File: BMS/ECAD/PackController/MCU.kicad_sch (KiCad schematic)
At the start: 51 parts, among them Q1 BC846, Q2 DMP4065S-7, U4 24LC256

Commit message: schematic finished, review tbd
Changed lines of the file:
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@@
+		)
+	)
+	(hierarchical_label "NTC1_Sig"
+		(shape input)
+		(at -19.05 182.88 180)
+		(effects
+			(font
+				(size 1.27 1.27)
+			)
+			(justify right)
 		)
 	)
@@
 		)
 	)
+	(hierarchical_label "NTC2_Sig"
+		(shape input)
+		(at -19.05 185.42 180)
+		(effects
+			(font
+				(size 1.27 1.27)
+			)
+			(justify right)
+		)
+	)
 	(hierarchical_label "UART_LS_TX"
 		(shape input)
@@
 		)
 	)
+	(hierarchical_label "NTC3_Sig"
+		(shape input)
+		(at -19.05 187.96 180)
+		(effects
+			(font
+				(size 1.27 1.27)
+			)
+			(justify right)
+		)
+	)
 	(hierarchical_label "AIR_P_Actual"
 		(shape input)
@@
 		)
 	)
+	(hierarchical_label "PCHRG_SWITCH"
+		(shape input)
+		(at -17.78 173.99 180)
+		(effects
+			(font
+				(size 1.27 1.27)
+			)
+			(justify right)
+		)
+	)
 	(hierarchical_label "Buzzer_CTRL"
 		(shape input)
@@
 		)
 	)
-	(hierarchical_label "DANGER_V"
+	(hierarchical_label "nDANGER_V"
 		(shape input)
 		(at -26.67 153.67 0)

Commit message: close to finish BMS master, only some footprints needed
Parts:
- removed D1, D2, D3, D4, D5: BAS16HT1, Diode_SMD:D_SOD-323_HandSoldering, symbol Diode:BAS16W
- removed Error1: LED Red, LED_SMD:LED_0805_2012Metric_Pad1.15x1.40mm_HandSolder, symbol Device:LED
- removed Heart?: LED Blue, LED_SMD:LED_0805_2012Metric_Pad1.15x1.40mm_HandSolder, symbol Device:LED
- removed R39: 1kR, Resistor_SMD:R_0603_1608Metric_Pad0.98x0.95mm_HandSolder, symbol Device:R
- removed R41, R42: 4.7kR, Resistor_SMD:R_0603_1608Metric_Pad0.98x0.95mm_HandSolder, symbol Device:R
- removed R9, R?: 100R 0603, Resistor_SMD:R_0603_1608Metric_Pad0.98x0.95mm_HandSolder, symbol Device:R
- removed R?: 20R 0603, Resistor_SMD:R_0603_1608Metric_Pad0.98x0.95mm_HandSolder, symbol Device:R
- added D201, D203, D204, D205, D206, D207, D209: BAT46, Diode_SMD:D_SOD-123, symbol Diode:BAT46
- added Error201: LED Red, LED_SMD:LED_0805_2012Metric_Pad1.15x1.40mm_HandSolder, symbol Device:LED
- added Heart201: LED Blue, LED_SMD:LED_0805_2012Metric_Pad1.15x1.40mm_HandSolder, symbol Device:LED
- added R203, R206, R208, R211, R213: 10kR, Resistor_SMD:R_0603_1608Metric_Pad0.98x0.95mm_HandSolder, symbol Device:R
- added R210, R212: 100R 0603, Resistor_SMD:R_0603_1608Metric_Pad0.98x0.95mm_HandSolder, symbol Device:R
- R214: renamed from R40; value 10kR -> 220kR
- U203: renamed from U6; value (none) -> SN74LVC1G74; footprint (none) -> Package_SO:VSSOP-8_2.3x2mm_P0.5mm
- U205: renamed from U4; value 24LC256 -> 24LC256-I/SN; footprint (none) -> Package_SO:SOIC-8_5.3x5.3mm_P1.27mm
- gave numbers to parts that had none: 22
- renumbered C20 to C208, C21 to C213, C19 to C214, Q2 to Q201, Q1 to Q202, R44 to R205, R43 to R207, R1 to R209, R2 to R216, R32 to R217, R33 to R218, R34 to R219, U5 to U202
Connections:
- net Heart_AFR is gone; now on net R_Leak1_Supply: U204.19 (PF2)
- net Reset_AFE is gone; now on net nRES: JTAG201.12 (Pin_12)
- net SC_Opening is gone; now on net SC_Latched: R214.1
- net +3.3V: now also R203.1, R206.1, R213.2
- net AIR_Error: now also U204.94 (PB7)
- net AIR_N_Actual: now also U204.93 (PB6)
- net AIR_N_Intended: now also U204.92 (PB5)
- net AIR_N_Switch: now also U204.86 (PD4)
- net AIR_P_Actual: now also U204.89 (PD7)
- net AIR_P_Intended: now also U204.88 (PD6)
- net AIR_P_Switch: now also U204.85 (PD3)
- net ERRQ: now also U204.61 (PD14)
- net ERRQ_Ioc_out: now also U204.57 (PD10)
- net ERRQ_ext: now also U204.59 (PD12)
- net ERRQ_ext_out: now also U204.58 (PD11)
- net ERRQ_res: now also U204.60 (PD13)
- net GND: now also R210.2, R211.1, R212.1
- net JTDO/SWO: now also U204.90 (PB3)
- net NTC1_Sig: now also U204.28 (PA6)
- net NTC2_Sig: now also U204.39 (PE8)
- net NTC3_Sig: now also U204.45 (PE14)
- net PCHRG_SWITCH: now also U204.82 (PD0)
- net R_Leak2_Supply: now also U204.18 (PC3)
- net SCL1: now also U204.30 (PC4); no longer U204.70 (PA9)
- net SC_State: now also D209.1 (K), R211.2
- net TSAL_GRN_ON: now also U204.9 (PC15)
- net UART_HS_TX: now also U204.70 (PA9); no longer U204.30 (PC4)
- net UART_LS_TX: now also U204.87 (PD5); no longer U204.22 (PA2)
- net V_ACCU: now also U204.40 (PE9)
- net V_VEHI: now also U204.22 (PA2)
- net WD_Beat: now also U204.97 (PE0)
- net WP1: now also U204.29 (PA7)
- net nDANGER_V: now also U204.26 (PA4)
- net nRES: now also U204.91 (PB4), D201.2 (A), D203.2 (A), R203.2; no longer U201.1 (~{RST}), U203.7 (nPRE)
- net nSleep: now also U204.62 (PD15)
- net nWDO: now also D203.1 (K), D206.1 (K)
- net at U203.6 (nCLR): now also D205.2 (A), D206.2 (A), D207.2 (A), R213.1
- net at U203.5 (Q): now also D209.2 (A), R208.2
- net at Q202.1 (B): now also R208.1
- net Heart: now reaches U204.1 (PE2)
- net Heart: now also Heart201.2 (A)
- net Error: now reaches U204.3 (PE4)
- net Error: now also Error201.2 (A)
- net Latch_SC: now reaches U204.65 (PC6)
- net Latch_SC: now also D205.1 (K)
- net nPOR_State: now reaches U204.66 (PC7)
- net nPOR_State: now also D204.2 (A), R206.2
- net SC_Latched: now reaches U204.67 (PC8)
- net SC_Latched: now also D207.1 (K)
- net nPRCHG_DONE: now reaches U204.83 (PD1)
- net PCHRG_ACTUAL: now reaches U204.84 (PD2)
- new net: Heart201.1 (K), R210.1
- new net: Error201.1 (K), R212.2
- new net nPOR: D201.1 (K), D204.1 (K), U201.1 (~{RST}), U203.7 (nPRE)
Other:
- note removed: "-> precharge act <- AIRP SW -> AIR P Power -> VAccu -> V Vehi für precharge logik TSAL logik bracuh nen haufen zeug"
- note removed: "Precharge, TSAl und HV Measuremeent müssen eigentlich mit drauf"
- moved on the sheet: C208, C209, C213, C214, Q201, Q202, R205, R207, R214, R217, R218, R219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

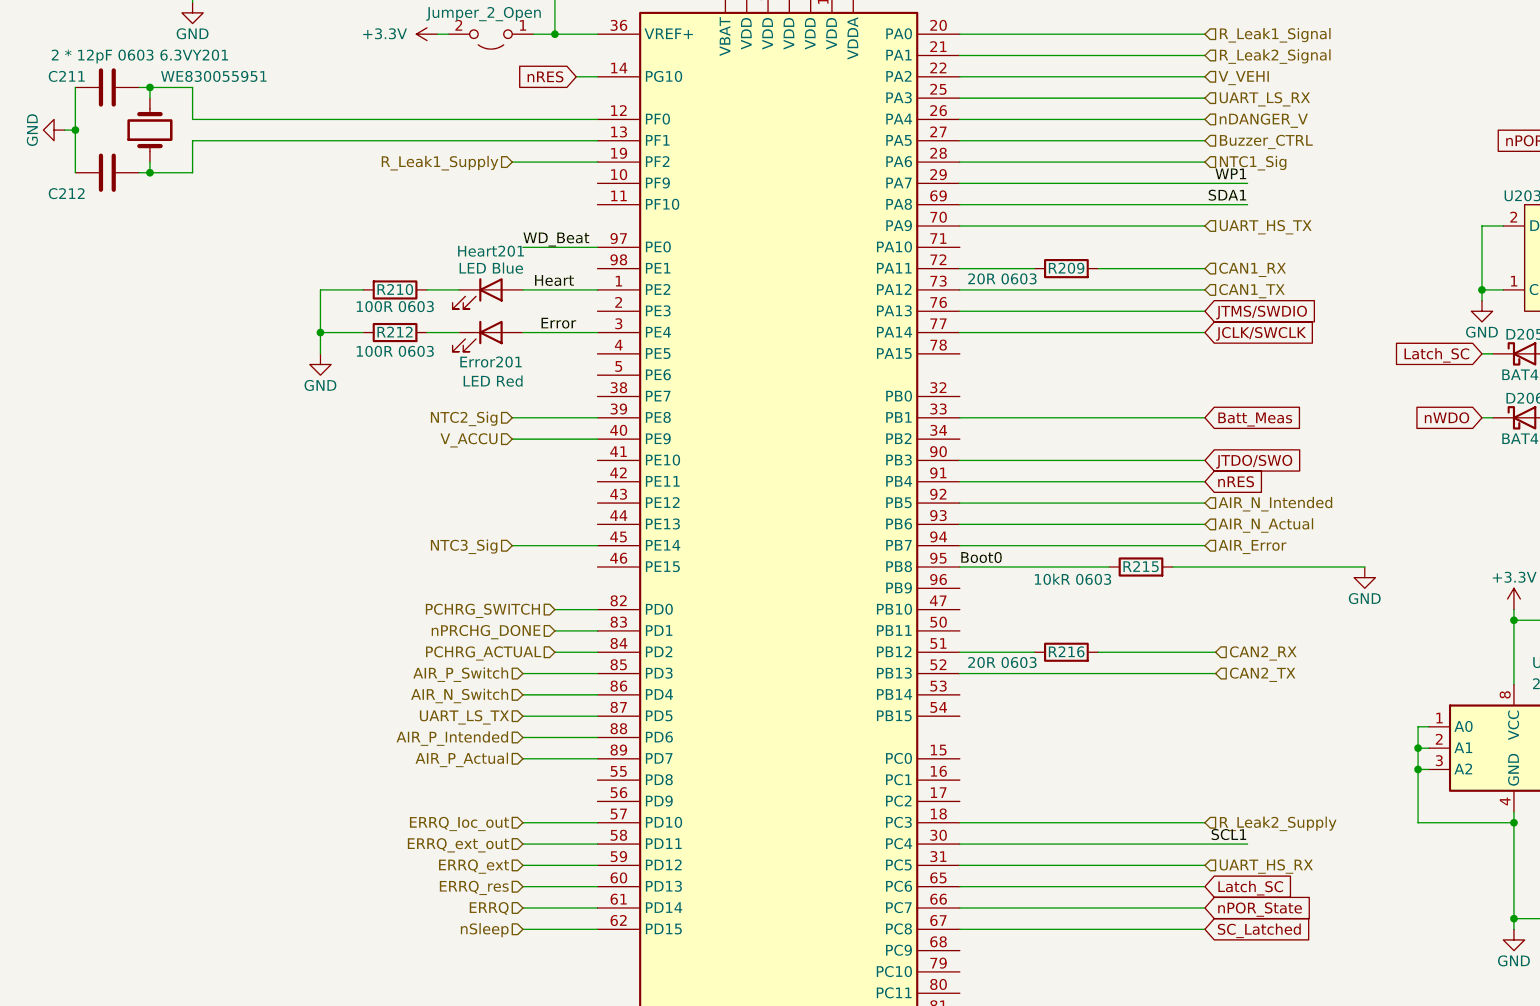
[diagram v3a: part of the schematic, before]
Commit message: Add several auxilary circuits to BMS Master
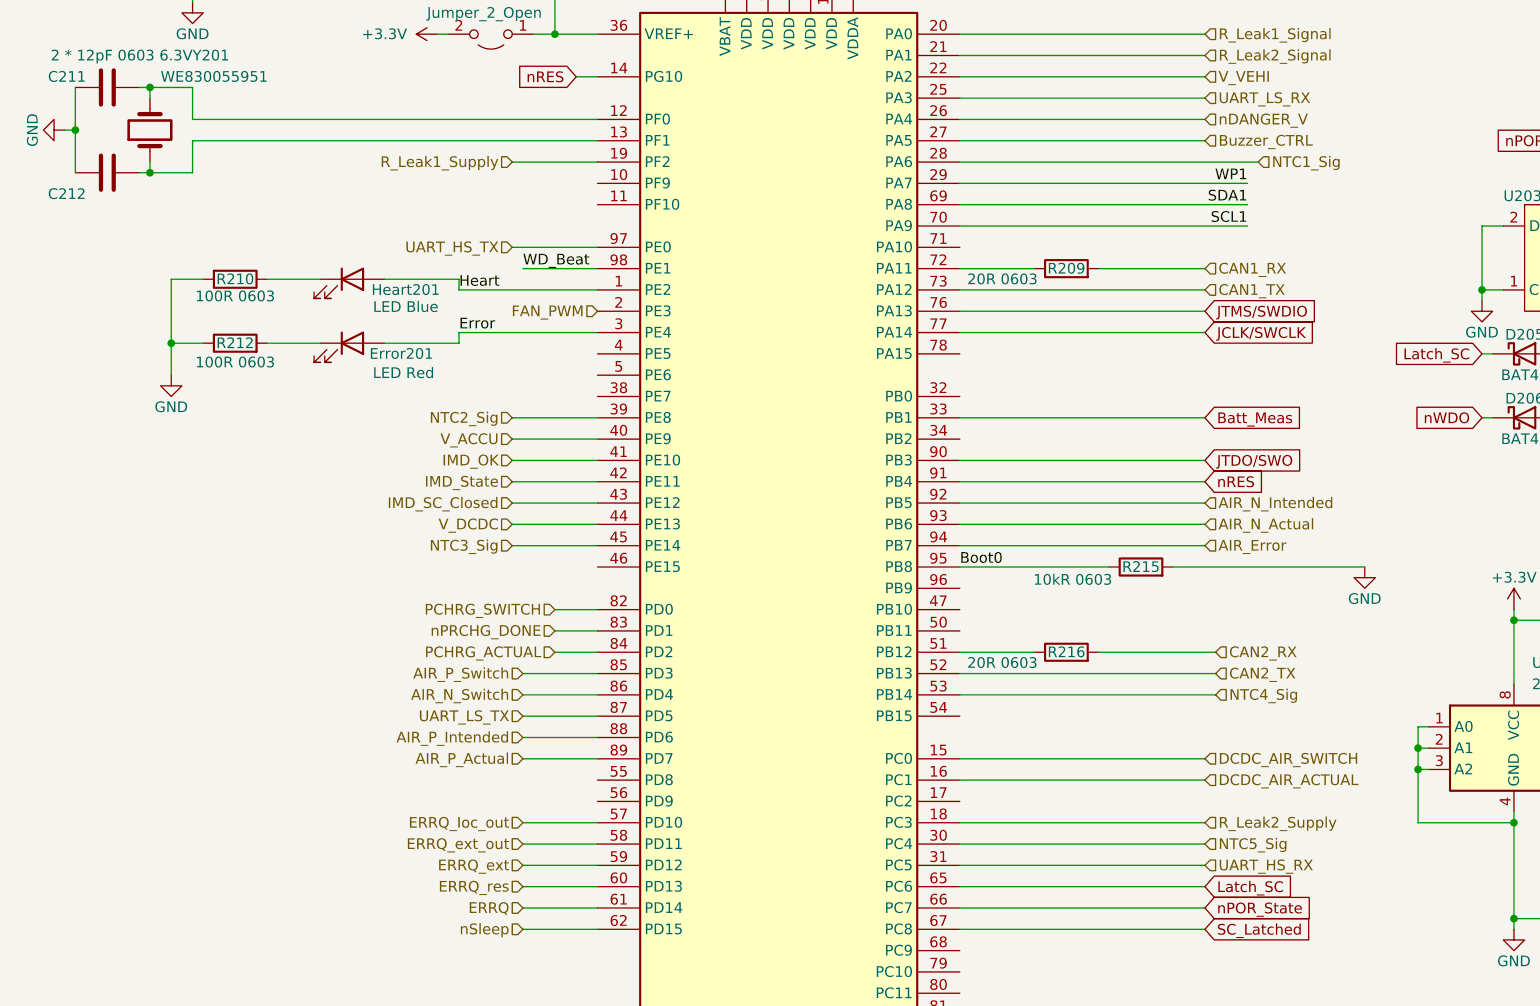
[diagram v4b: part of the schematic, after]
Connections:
- net SCL1: now also U204.70 (PA9); no longer U204.30 (PC4)
- net UART_HS_TX: now also U204.97 (PE0); no longer U204.70 (PA9)
- net WD_Beat: now also U204.98 (PE1); no longer U204.97 (PE0)
- net DCDC_AIR_SWITCH: now reaches U204.15 (PC0)
- net DCDC_AIR_ACTUAL: now reaches U204.16 (PC1)
- net FAN_PWM: now reaches U204.2 (PE3)
- net IMD_OK: now reaches U204.41 (PE10)
- net IMD_State: now reaches U204.42 (PE11)
- net IMD_SC_Closed: now reaches U204.43 (PE12)
- net V_DCDC: now reaches U204.44 (PE13)
- net NTC4_Sig: now reaches U204.53 (PB14)
- new net NTC5_Sig: U204.30 (PC4)
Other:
- moved on the sheet: Error201, Heart201, R210, R212
